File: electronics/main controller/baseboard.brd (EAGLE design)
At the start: 75 x 30 mm, 45 parts, among them J1 2.1MMJACKTHM, J2 M02PTH, U1 ATMEGA328P, X1 16MHz

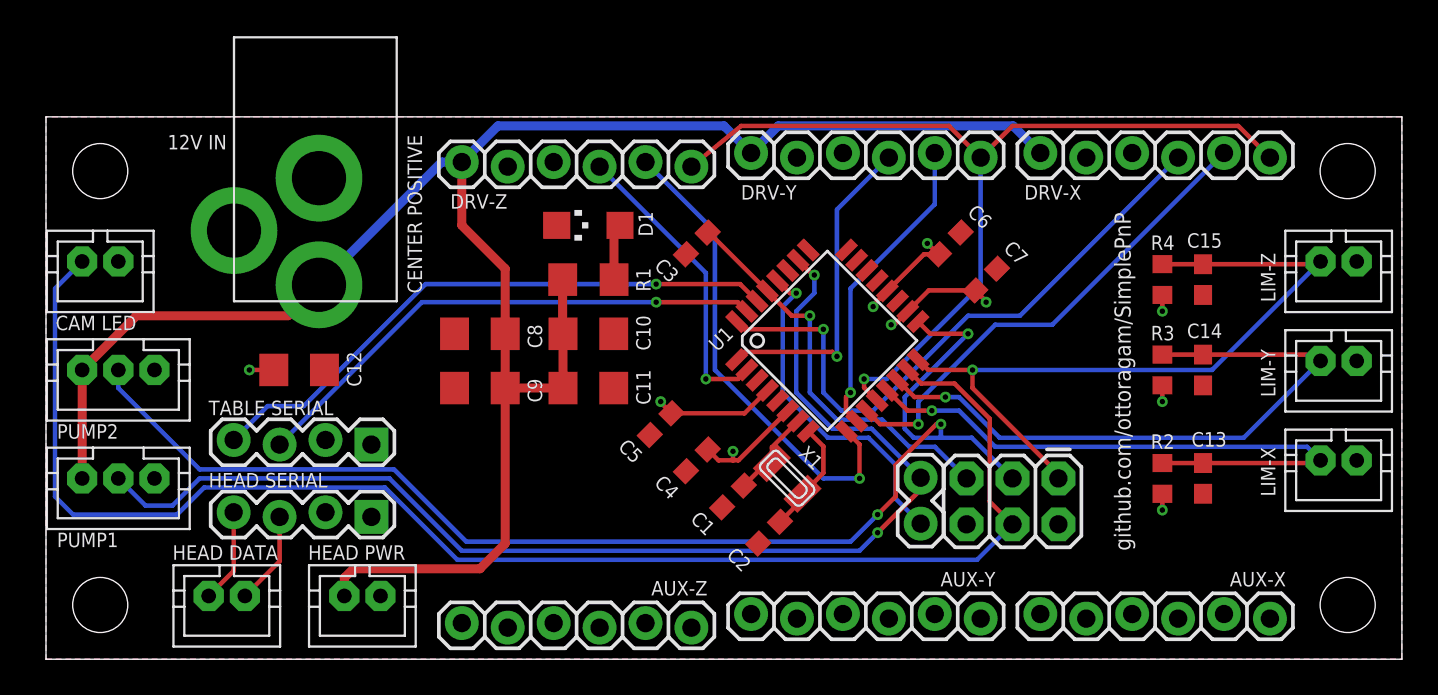
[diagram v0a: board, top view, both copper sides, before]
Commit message: updated all PCBs and added PDF schematics
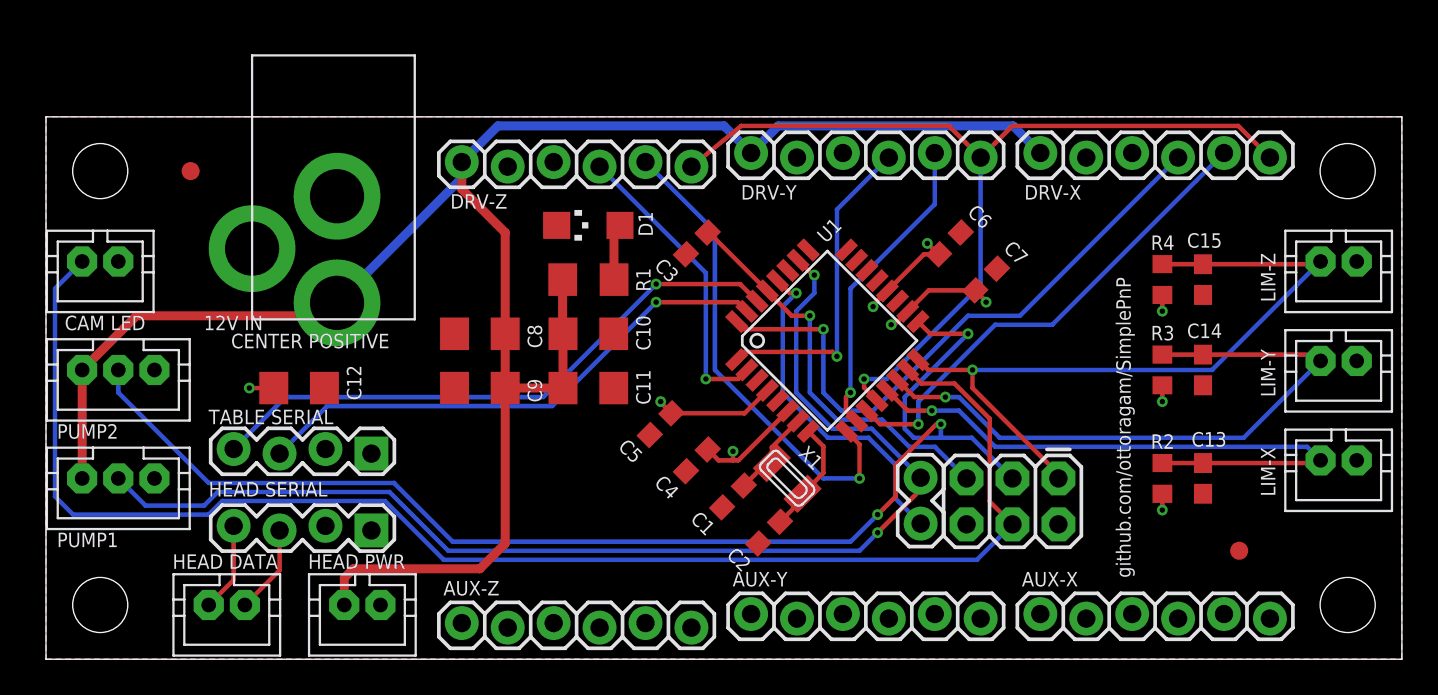
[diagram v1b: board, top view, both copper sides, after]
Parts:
- added U$1, U$2: FIDUCIAL, adafruit:FIDUCIAL_1MM
- moved J1 1.41 mm to (16.0, 29.0)
- moved C12 1.00 mm to (14.0, 15.0)
- moved HEAD-SERIAL 0.75 mm to (18.0, 7.25)
- moved HEAD-DATA 0.50 mm to (10.0, 3.00)
- moved HEAD-PWR 0.50 mm to (17.5, 3.00)
- moved TABLE-SERIAL 0.50 mm to (18.0, 11.5)
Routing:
- net 12V: track 108.5 -> 109.5 mm
- net PWMSPINDLE: track 82.1 -> 81.5 mm
- net COOLANT: track 66.3 -> 65.7 mm
